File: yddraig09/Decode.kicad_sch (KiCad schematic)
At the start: 15 parts, among them U10 74LS138, U11 74LS21, U12 74LS245, U13 74LS138, U14 74LS139, U8 74LS245, U9 74LS245

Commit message: Some changes
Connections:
- net ~{BANKSEL}: no longer U13.15 (O0)
- net ~{CS_IRQEN}: no longer U13.14 (O1)
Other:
- note added: "Merge the Bank select and IRQ signals IRQ on 0x00-0x7F BankSel on 0x80 - 0xFF Change one of the spare selects to use for the IDE controller"
- moved on the sheet: C23, C24, C25, C26, C27, C28, C29, C30, U14A

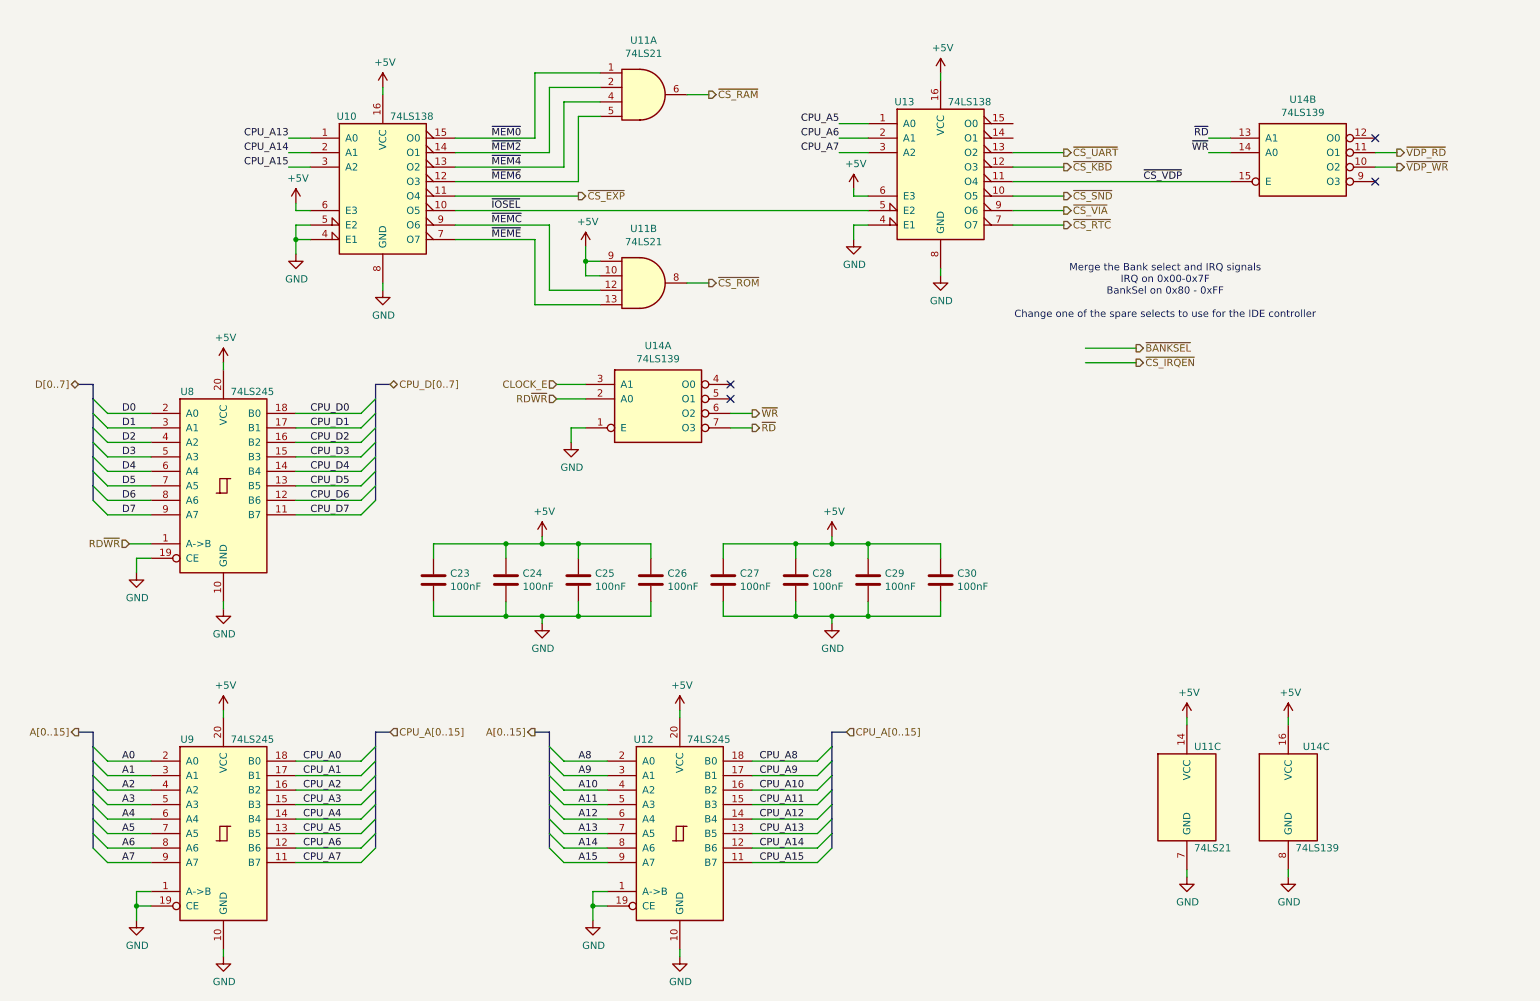
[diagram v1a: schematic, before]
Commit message: Finished changes to 6809 schematics
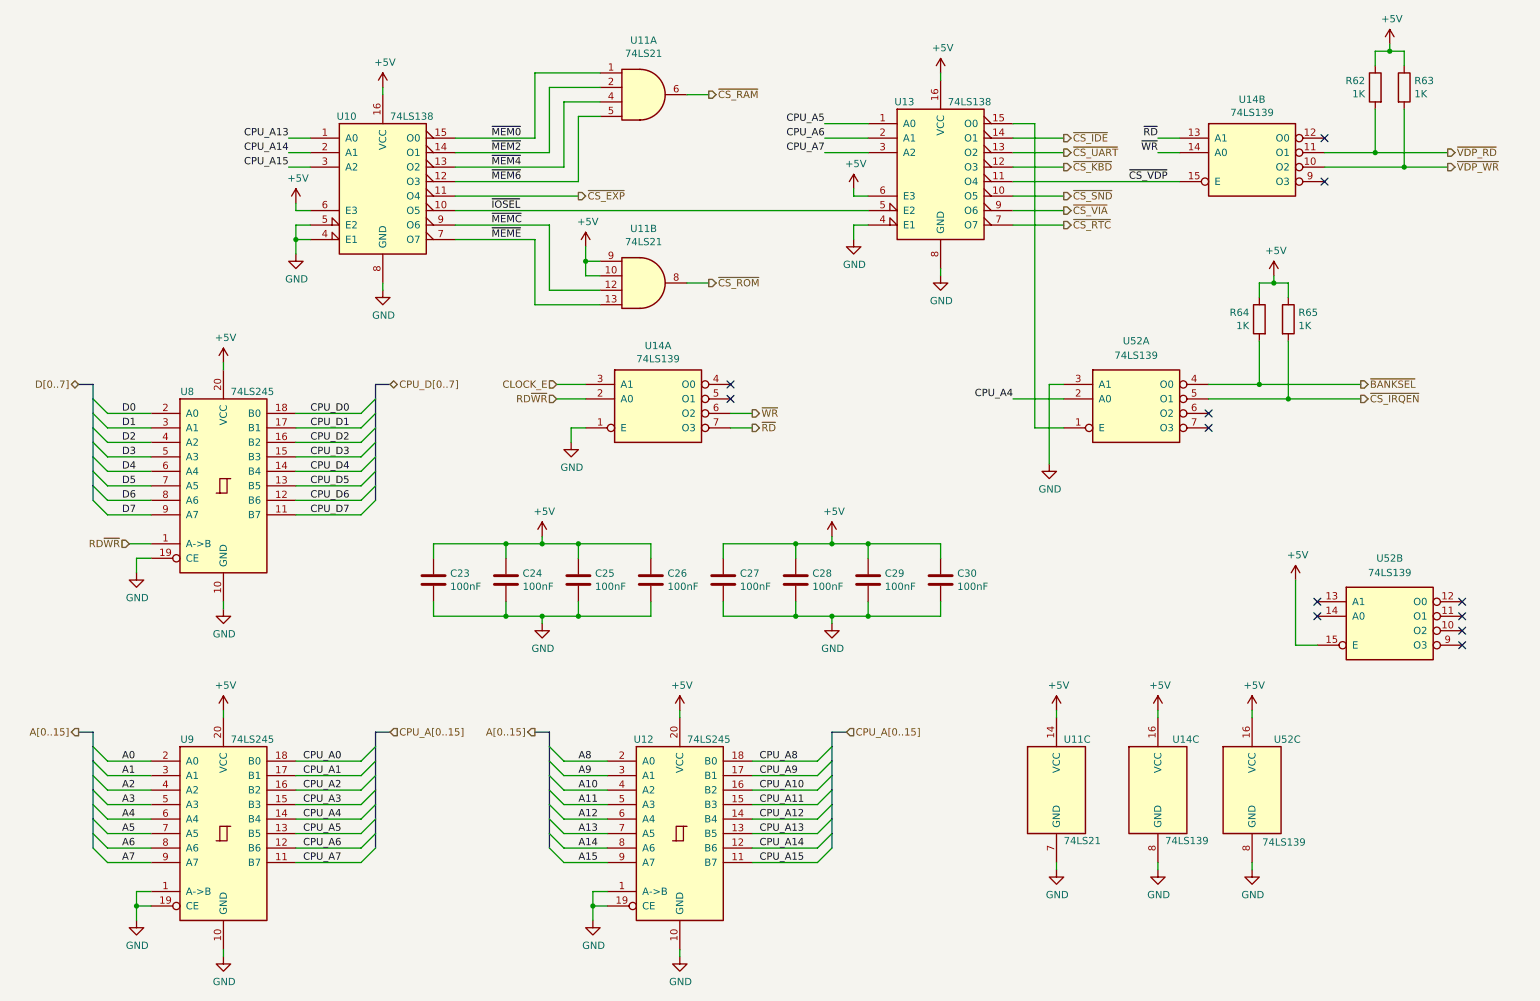
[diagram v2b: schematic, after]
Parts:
- added R62, R63, R64, R65: 1K, Resistor_THT:R_Axial_DIN0207_L6.3mm_D2.5mm_P10.16mm_Horizontal, symbol Device:R
- added U52: 74LS139, symbol 74xx:74LS139
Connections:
- net +5V: now also R62.1, R63.1, R64.1, R65.1, U52.15 (E), U52.16 (VCC)
- net CPU_A4: now also U52.2 (A0)
- net GND: now also U52.3 (A1), U52.8 (GND)
- net ~{BANKSEL}: now also R64.2, U52.4 (O0)
- net ~{CS_IRQEN}: now also R65.2, U52.5 (O1)
- net ~{VDP_RD}: now also R62.2
- net ~{VDP_WR}: now also R63.2
- net ~{CS_IDE}: now reaches U13.14 (O1)
- net at U13.15 (O0): now also U52.1 (E)
- no-connect marks 4 -> 12
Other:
- note removed: "Merge the Bank select and IRQ signals IRQ on 0x00-0x7F BankSel on 0x80 - 0xFF Change one of the spare selects to use for the IDE controller"
- moved on the sheet: U11C, U14B, U14C

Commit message: 6809 board changes
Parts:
- U15: renamed from U52; footprint (none) -> Package_DIP:DIP-16_W7.62mm_Socket
- renumbered R64 to R20, R65 to R21, R62 to R22, R63 to R23, U14 to U12, U12 to U13, U13 to U14

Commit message: More changes
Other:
- note added: "Address Banks: 0x0000-0x7FFF RAM 0x8000-0x8000 Expansion 0xA000-0xBFFF I/O 0xC000-0xFFFF ROM"
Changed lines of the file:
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@@
 	(wire
 		(pts
-			(xy 262.89 41.91) (xy 275.59 41.91)
+			(xy 262.89 41.91) (xy 273.05 41.91)
 		)
 		(stroke
@@
 	(wire
 		(pts
-			(xy 267.97 44.45) (xy 275.59 44.45)
+			(xy 267.97 44.45) (xy 273.05 44.45)
 		)
 		(stroke
@@
 			(width 0)
 			(type default)
+		)
+	)
+	(text "Address Banks:\n0x0000-0x7FFF RAM\n0x8000-0x8000 Expansion\n0xA000-0xBFFF I/O\n0xC000-0xFFFF ROM"
+		(exclude_from_sim no)
+		(at 59.69 27.178 0)
+		(effects
+			(font
+				(size 1.27 1.27)
+			)
+			(justify left)
 		)
 	)
@@
 	(hierarchical_label "~{VDP_WR}"
 		(shape output)
-		(at 275.59 44.45 0)
+		(at 273.05 44.45 0)
 		(fields_autoplaced yes)
 		(effects
@@
 	(hierarchical_label "~{VDP_RD}"
 		(shape output)
-		(at 275.59 41.91 0)
-		(fields_autoplaced yes)
-		(effects
+		(at 273.05 41.91 0)
+		(fields_autoplaced yes)
+		(effects

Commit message: BOard changes
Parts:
- removed R20, R21: 1K, Resistor_THT:R_Axial_DIN0207_L6.3mm_D2.5mm_P10.16mm_Horizontal, symbol Device:R
- removed U15: 74LS139, Package_DIP:DIP-16_W7.62mm_Socket, symbol 74xx:74LS139
- renumbered R22 to R20, R23 to R21, U13 to U12, U14 to U13, U12 to U14
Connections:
- net ~{CS_RTC} is gone; now on net ~{CS_IRQEN}: U13.7 (O7)
- net ~{BANKSEL}: now also U13.15 (O0)
- no-connect marks 12 -> 4
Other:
- note added: "0xA000-0xA01F - BANK SELECT 0xA020-0xA03F - IDE 0xA040-0xA07F - SERIAL 0xA060-0xA07F - KEYBOARD 0xA080-0xA09F - VIDEO 0xA0A0-0xA0BF - SOUND 0xA0C0-0xA0CF - 65C22 VIA 0xA0E0-0xA0FF - INTERRUPT CONTROL"
- moved on the sheet: U14A
